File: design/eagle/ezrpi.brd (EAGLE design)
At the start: 65 x 56 mm, 40 parts

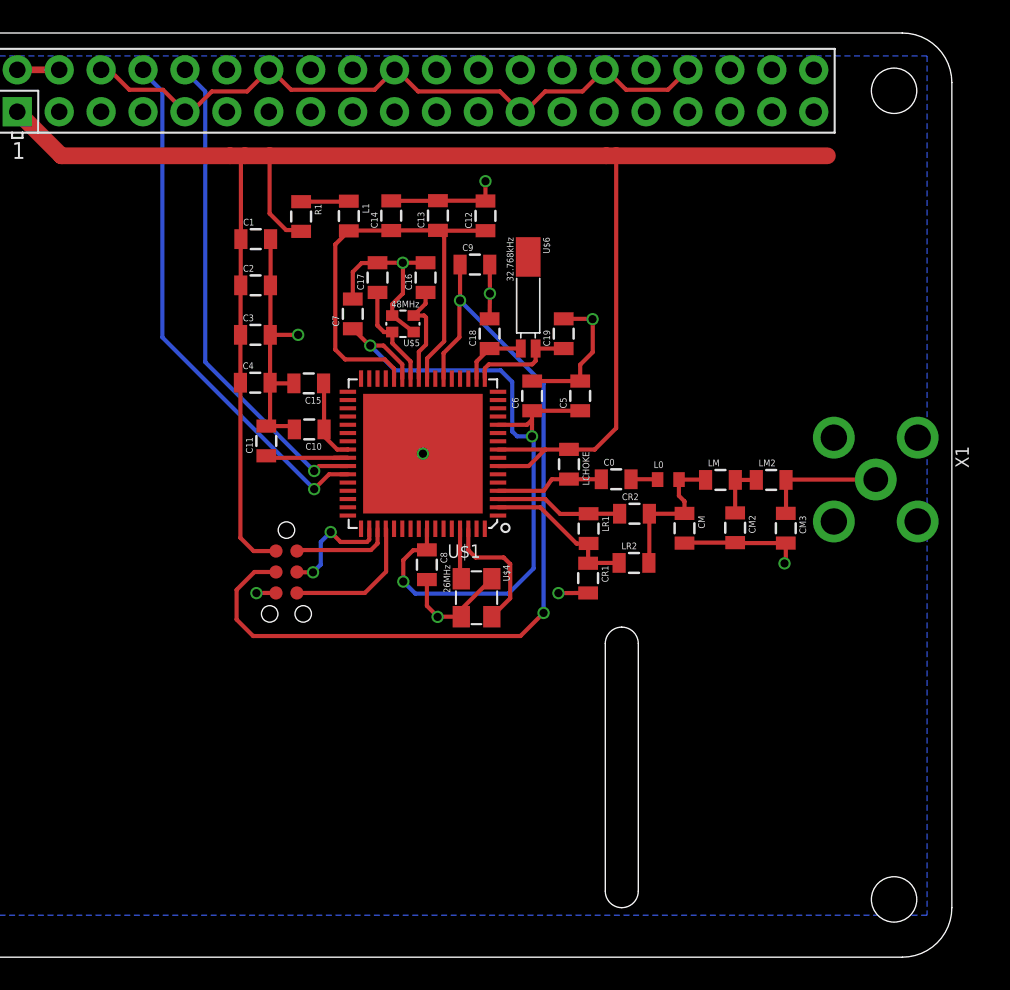
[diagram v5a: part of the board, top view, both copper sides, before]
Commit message: added top ground plane, fixed silk & naming
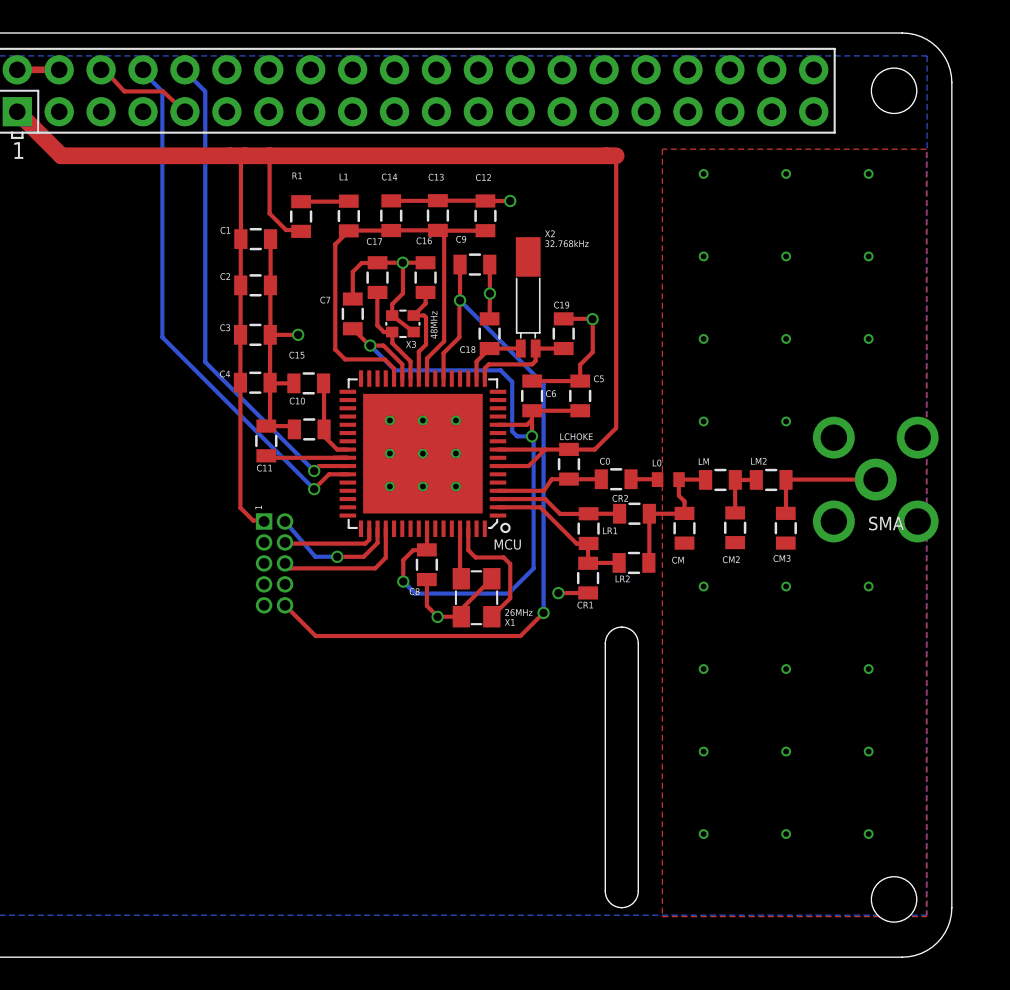
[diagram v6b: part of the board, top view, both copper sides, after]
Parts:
- removed U$3: JTAG-6PINS, setup:TC2030-IDC
- removed U$4: 26MHz, xtal:ABM8
- added SMA: (no value), connector:SMA90_DIP
- added SWD: FTSH2X5, connector:HEADER2X5
- X1: value (none) -> 26MHz; device connector:SMA90_DIP -> xtal:ABM8
- moved X1 25.2 mm to (38.7, 24.3)
- renumbered U$1 to MCU, U$2 to RPI, U$5 to X3, U$6 to X2
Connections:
- net GND: now also SMA.GND1, SMA.GND2, SMA.GND3, SMA.GND4, SWD.P$3, SWD.P$5, SWD.P$9, X1.2, X1.4; no longer U$3.5, U$4.2, U$4.4, X1.GND1, X1.GND2, X1.GND3, X1.GND4
- net N$1: now also SMA.ANTENNA; no longer X1.ANTENNA
- net RESET: now also SWD.P$10; no longer U$3.3
- net SWCLK: now also SWD.P$4; no longer U$3.4
- net SWDIO: now also SWD.P$2; no longer U$3.2
- net SWO: now also SWD.P$6; no longer U$3.6
- net VCC: now also SWD.P$1; no longer U$3.1
- net XIN: now also X1.1; no longer U$4.1
- net XOUT: now also X1.3; no longer U$4.3
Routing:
- net GND: track 106.1 -> 62.2 mm, vias 10 -> 39
- net VCC: track 109.5 -> 94.2 mm
- net RESET: track 52.6 -> 45.4 mm
- net SWDIO: track 5.97 -> 7.80 mm, vias 0 -> 1
- net SWCLK: track 7.17 -> 5.89 mm, vias 2 -> 0
- added copper zone on layer 1, net GND
